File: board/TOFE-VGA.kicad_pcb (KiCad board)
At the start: 2 copper layers, 1 part

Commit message: Started rough layout of pcb
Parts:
- removed U?: TOFE_VGA_Expansion_Board_8x_FullHeight, TOFE_8X_FullHeight
- added C201, C202, C203, C216, C218: 22u, Capacitors_SMD:c_elec_4x5.8, F.Cu at (70.1, 247.0)
- added C204, C205, C206, C207, C208, C209, C210, C211, C212, C213, C219, C220, C221, C301: 100n, Resistors_SMD:R_0805_HandSoldering, F.Cu at (70.1, 247.0)
- added C214: 1u, Capacitors_SMD:c_elec_4x5.8, F.Cu at (70.1, 247.0)
- added C215, C409: 10n, Resistors_SMD:R_0805_HandSoldering, F.Cu at (70.1, 247.0)
- added C217: 2u2, Capacitors_SMD:c_elec_4x5.8, F.Cu at (70.1, 247.0)
- added C401, C402, C403, C404, C405, C406, C407, C408: 47n, Resistors_SMD:R_0805_HandSoldering, F.Cu at (70.1, 247.0)
- added C410: 82n, Resistors_SMD:R_0805_HandSoldering, F.Cu at (100.2, 93.0)
- added C411: 8.2n, Resistors_SMD:R_0805_HandSoldering, F.Cu at (104.2, 93.0)
- added D201, D202, D203, D204, D205, D302, D303, D304: LED, LEDs:LED_0805, F.Cu at (70.1, 247.0)
- added D301: DIODE, Diodes_SMD:SMB_Handsoldering, F.Cu at (70.1, 247.0)
- added JP301: JUMPER, CON-SMD-2.54:HARWIN-M20-87-2x1, F.Cu at (70.1, 247.0)
- added L401, L402, L403, L404, L405, L406: FERRITE, Resistors_SMD:R_0805_HandSoldering, F.Cu at (70.1, 247.0)
- added P301: TOFE I2C, CON-SMD-2.54:HARWIN-M20-87-4x1, F.Cu at (70.1, 247.0)
- added P302: TOFE-8X, TOFE_8X_HalfHeight:TOFE_8X_HalfHeight, F.Cu at (62.2, 154.0)
- added P303: DEBUG, CON-SMD-2.54:TE-AMPMODU-MOD-II-4X2, F.Cu at (102.2, 137.0)
- added P401: AD9984 I2C, CON-SMD-2.54:HARWIN-M20-87-4x1, F.Cu at (130.2, 93.0)
- added P501: VGA RX I2C 3v, CON-SMD-2.54:HARWIN-M20-87-4x1, F.Cu at (70.1, 247.0)
- added P502: VGA TX I2C 3v, CON-SMD-2.54:HARWIN-M20-87-4x1, F.Cu at (70.1, 247.0)
- added P503: VGA RX I2C 5v, CON-SMD-2.54:HARWIN-M20-87-4x1, F.Cu at (70.1, 247.0)
- added P504: VGA TX I2C 5v, CON-SMD-2.54:HARWIN-M20-87-4x1, F.Cu at (70.1, 247.0)
- added P505: DE-15, DE-15:TE-1-1734530-1, F.Cu at (62.2, 120.0)
- added P506: DE-15, DE-15:TE-1-1734530-1, F.Cu at (62.2, 85.0)
- added P601: 3-RCA, 3-RCA:MR-100H, F.Cu at (119.2, 60.0)
- added R201: 470R, Resistors_SMD:R_0805_HandSoldering, F.Cu at (70.1, 247.0)
- added R202, R206: 76K8, Resistors_SMD:R_0805_HandSoldering, F.Cu at (70.1, 247.0)
- added R203, R207: 147K, Resistors_SMD:R_0805_HandSoldering, F.Cu at (70.1, 247.0)
- added R204, R304, R305, R306: 68R, Resistors_SMD:R_0805_HandSoldering, F.Cu at (70.1, 247.0)
- added R205, R209: 1R8, Resistors_SMD:R_0805_HandSoldering, F.Cu at (70.1, 247.0)
- added R208: 150R, Resistors_SMD:R_0805_HandSoldering, F.Cu at (70.1, 247.0)
- added R301, R302, R303: 10K, Resistors_SMD:R_0805_HandSoldering, F.Cu at (70.1, 247.0)
- added R401, R402, R403, R404, R405, R406: 75R, Resistors_SMD:R_0805_HandSoldering, F.Cu at (70.1, 247.0)
- added R407: 1K, Resistors_SMD:R_0805_HandSoldering, F.Cu at (70.1, 247.0)
- added R408: 10K, Resistors_SMD:R_0805_HandSoldering, F.Cu at (112.2, 129.0)
- added R409: 10K, Resistors_SMD:R_0805_HandSoldering, F.Cu at (115.2, 132.0)
- added R410: 1K5, Resistors_SMD:R_0805_HandSoldering, F.Cu at (100.2, 99.0)
- added R411: 1K, Resistors_SMD:R_0805_HandSoldering, F.Cu at (111.2, 94.0)
- added R412: 1K, Resistors_SMD:R_0805_HandSoldering, F.Cu at (115.2, 94.0)
- added R413: 1K, Resistors_SMD:R_0805_HandSoldering, F.Cu at (118.2, 94.0)
- added R414: 1K, Resistors_SMD:R_0805_HandSoldering, F.Cu at (121.2, 94.0)
- added R415: 2k2, Resistors_SMD:R_0805_HandSoldering, F.Cu at (127.2, 86.0)
- added R416: 2K2, Resistors_SMD:R_0805_HandSoldering, F.Cu at (131.2, 85.0)
- added R501, R502, R503, R504: 2K2, Resistors_SMD:R_0805_HandSoldering, F.Cu at (70.1, 247.0)
- added R505, R506, R507, R508: 4K7, Resistors_SMD:R_0805_HandSoldering, F.Cu at (70.1, 247.0)
- added TP401, TP402, TP404: TESTPOINT, SMD_Packages:1Pin, F.Cu at (70.1, 247.0)
- added TP403: TESTPOINT, SMD_Packages:1Pin, F.Cu at (107.2, 184.0)
- added U201, U202: ADP3334, Housings_SSOP:MSOP-8_3x3mm_Pitch0.65mm, F.Cu at (70.1, 247.0)
- added U203: LP2985, TO_SOT_Packages_SMD:SOT-23-5, F.Cu at (70.1, 247.0)
- added U301: 24AA01/24LC01B, TO_SOT_Packages_SMD:SOT-23-5, F.Cu at (70.1, 247.0)
- added U401: AD9984, analog-devices2:analog-devices2-LQFP80, F.Cu at (119.2, 114.0)
- added U501, U502: TCA9617A, Housings_SSOP:MSOP-8_3x3mm_Pitch0.65mm, F.Cu at (70.1, 247.0)
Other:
- board outline added: 46 x 3 mm
- copper layers 2 -> 4
- board text added: "99 x 99mm"

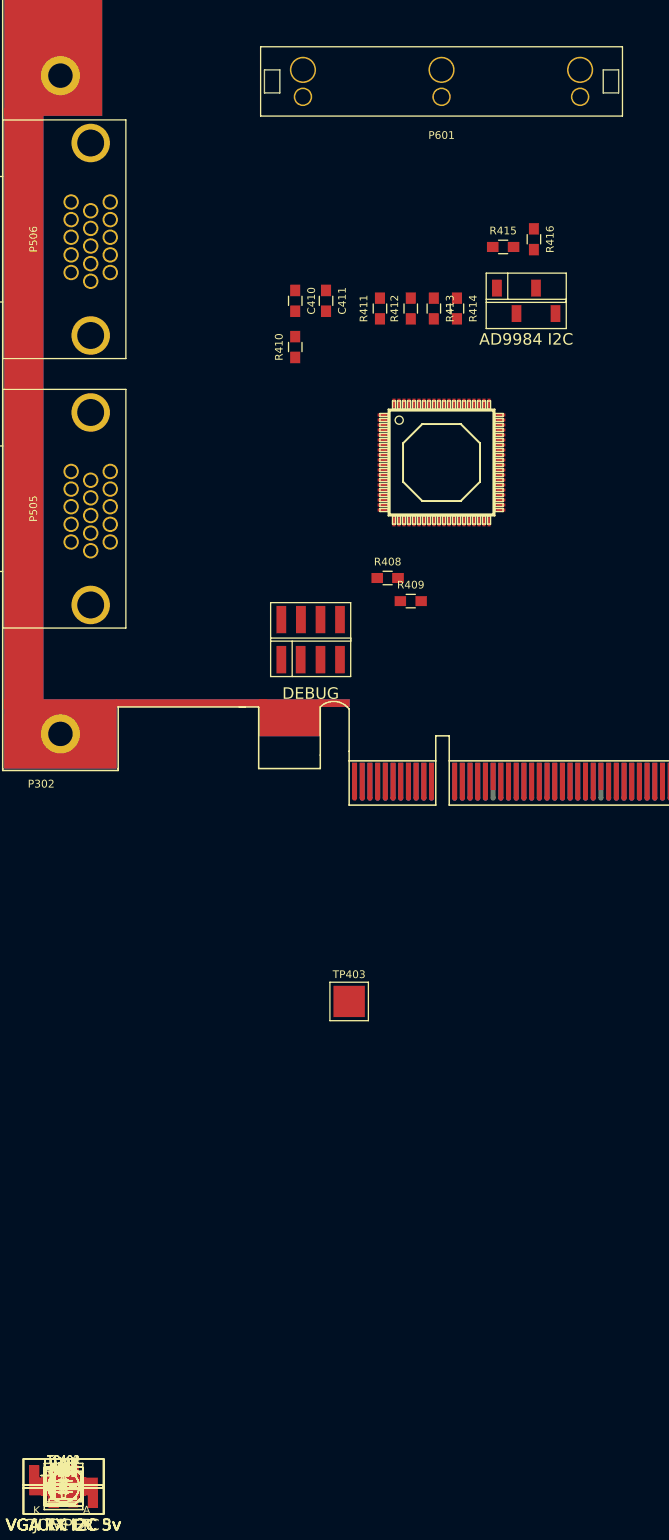
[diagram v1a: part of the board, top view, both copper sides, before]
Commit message: Remove component input to allow design to fit on smaller and much cheaper board
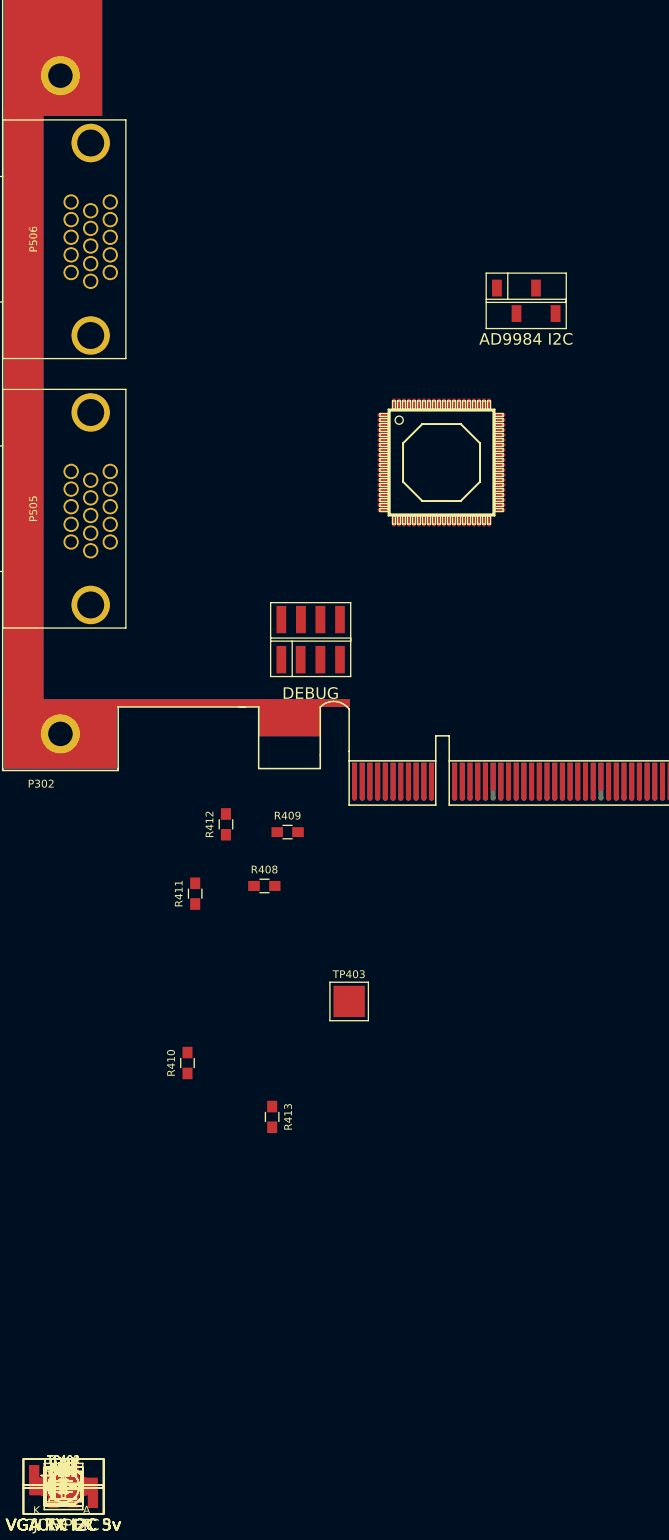
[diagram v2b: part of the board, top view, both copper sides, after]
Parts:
- removed C408: 47n, Resistors_SMD:R_0805_HandSoldering
- removed C409: 10n, Resistors_SMD:R_0805_HandSoldering
- removed C410: 82n, Resistors_SMD:R_0805_HandSoldering
- removed C411: 8.2n, Resistors_SMD:R_0805_HandSoldering
- removed L404, L405, L406: FERRITE, Resistors_SMD:R_0805_HandSoldering
- removed P601: 3-RCA, 3-RCA:MR-100H
- removed R414: 1K, Resistors_SMD:R_0805_HandSoldering
- removed R415: 2k2, Resistors_SMD:R_0805_HandSoldering
- removed R416: 2K2, Resistors_SMD:R_0805_HandSoldering
- C405: value 47n -> 10n
- C406: value 47n -> 82n
- C407: value 47n -> 8.2n
- R404: value 75R -> 1K
- R405, R406: value 75R -> 10K
- R407: value 1K -> 1K5
- R408, R409: value 10K -> 1K
- R410: value 1K5 -> 1K
- R412: value 1K -> 2k2
- R413: value 1K -> 2K2
- moved R413 107.1 mm to (97.2, 199.0)
- moved R410 94.0 mm to (86.2, 192.0)
- moved R411 79.7 mm to (87.2, 170.0)
- moved R412 71.2 mm to (91.2, 161.0)
- moved R408 43.1 mm to (96.2, 169.0)
- moved R409 34.0 mm to (99.2, 162.0)
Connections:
- C403 pad 2: Net-(C403-Pad2) -> Net-(C402-Pad2)
- C404 pad 2: Net-(C403-Pad2) -> Net-(C404-Pad2)
- C406 pad 1: Net-(C406-Pad1) -> PVD
- C406 pad 2: Net-(C405-Pad2) -> Net-(C406-Pad2)
- C407 pad 1: Net-(C407-Pad1) -> PVD
- L402 pad 1: /TOFE-VGA/AD9984/COMP_Pb -> /TOFE-VGA/AD9984/VGA_G
- L403 pad 1: /TOFE-VGA/AD9984/VGA_G -> /TOFE-VGA/AD9984/VGA_R
- L403 pad 2: Net-(C403-Pad2) -> Net-(C404-Pad2)
- R403 pad 1: Net-(C403-Pad2) -> Net-(C404-Pad2)
- R404 pad 1: Net-(C405-Pad2) -> Net-(R404-Pad1)
- R405 pad 1: Net-(C407-Pad2) -> +3V3
- R405 pad 2: GND -> /TOFE-VGA/AD9984/VSOUT
- R406 pad 1: Net-(C408-Pad2) -> /TOFE-VGA/AD9984/VSOUT
- R407 pad 1: Net-(R407-Pad1) -> Net-(C407-Pad2)
- R407 pad 2: GND -> Net-(C406-Pad2)
- R408 pad 1: +3V3 -> Net-(R408-Pad1)
- R408 pad 2: /TOFE-VGA/AD9984/VSOUT -> GND
- R409 pad 1: /TOFE-VGA/AD9984/VSOUT -> Net-(R409-Pad1)
- R410 pad 1: Net-(C411-Pad2) -> GND
- R410 pad 2: Net-(C410-Pad2) -> Net-(R410-Pad2)
- R411 pad 1: Net-(R411-Pad1) -> GND
- R411 pad 2: GND -> Net-(R411-Pad2)
- R412 pad 1: Net-(R412-Pad1) -> +3V3
- R412 pad 2: GND -> /TOFE-VGA/AD9984/SCL_AD9984
- R413 pad 1: GND -> +3V3
- R413 pad 2: Net-(R413-Pad2) -> /TOFE-VGA/AD9984/SDA_AD9984
- TP401 pad 1: Net-(R407-Pad1) -> Net-(R404-Pad1)
- TP403 pad 1: Net-(R411-Pad1) -> Net-(R408-Pad1)
- TP404 pad 1: Net-(R412-Pad1) -> Net-(R409-Pad1)
- U401 pad 10: Net-(C405-Pad1) -> Net-(U401-Pad10)
- U401 pad 12: Net-(C406-Pad1) -> Net-(U401-Pad12)
- U401 pad 14: Net-(C407-Pad1) -> Net-(C404-Pad1)
- U401 pad 17: Net-(R407-Pad1) -> Net-(R404-Pad1)
- U401 pad 18: Net-(C409-Pad2) -> Net-(C405-Pad2)
- U401 pad 20: Net-(C409-Pad1) -> Net-(C405-Pad1)
- U401 pad 4: Net-(C402-Pad1) -> Net-(U401-Pad4)
- U401 pad 6: Net-(C403-Pad1) -> Net-(C402-Pad1)
- U401 pad 68: Net-(R414-Pad2) -> Net-(R411-Pad2)
- U401 pad 69: Net-(R413-Pad2) -> Net-(R410-Pad2)
- U401 pad 72: Net-(R412-Pad1) -> Net-(R409-Pad1)
- U401 pad 73: Net-(R411-Pad1) -> Net-(R408-Pad1)
- U401 pad 78: Net-(C411-Pad2) -> Net-(C407-Pad2)
- U401 pad 8: Net-(C404-Pad1) -> Net-(C403-Pad1)
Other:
- board outline removed

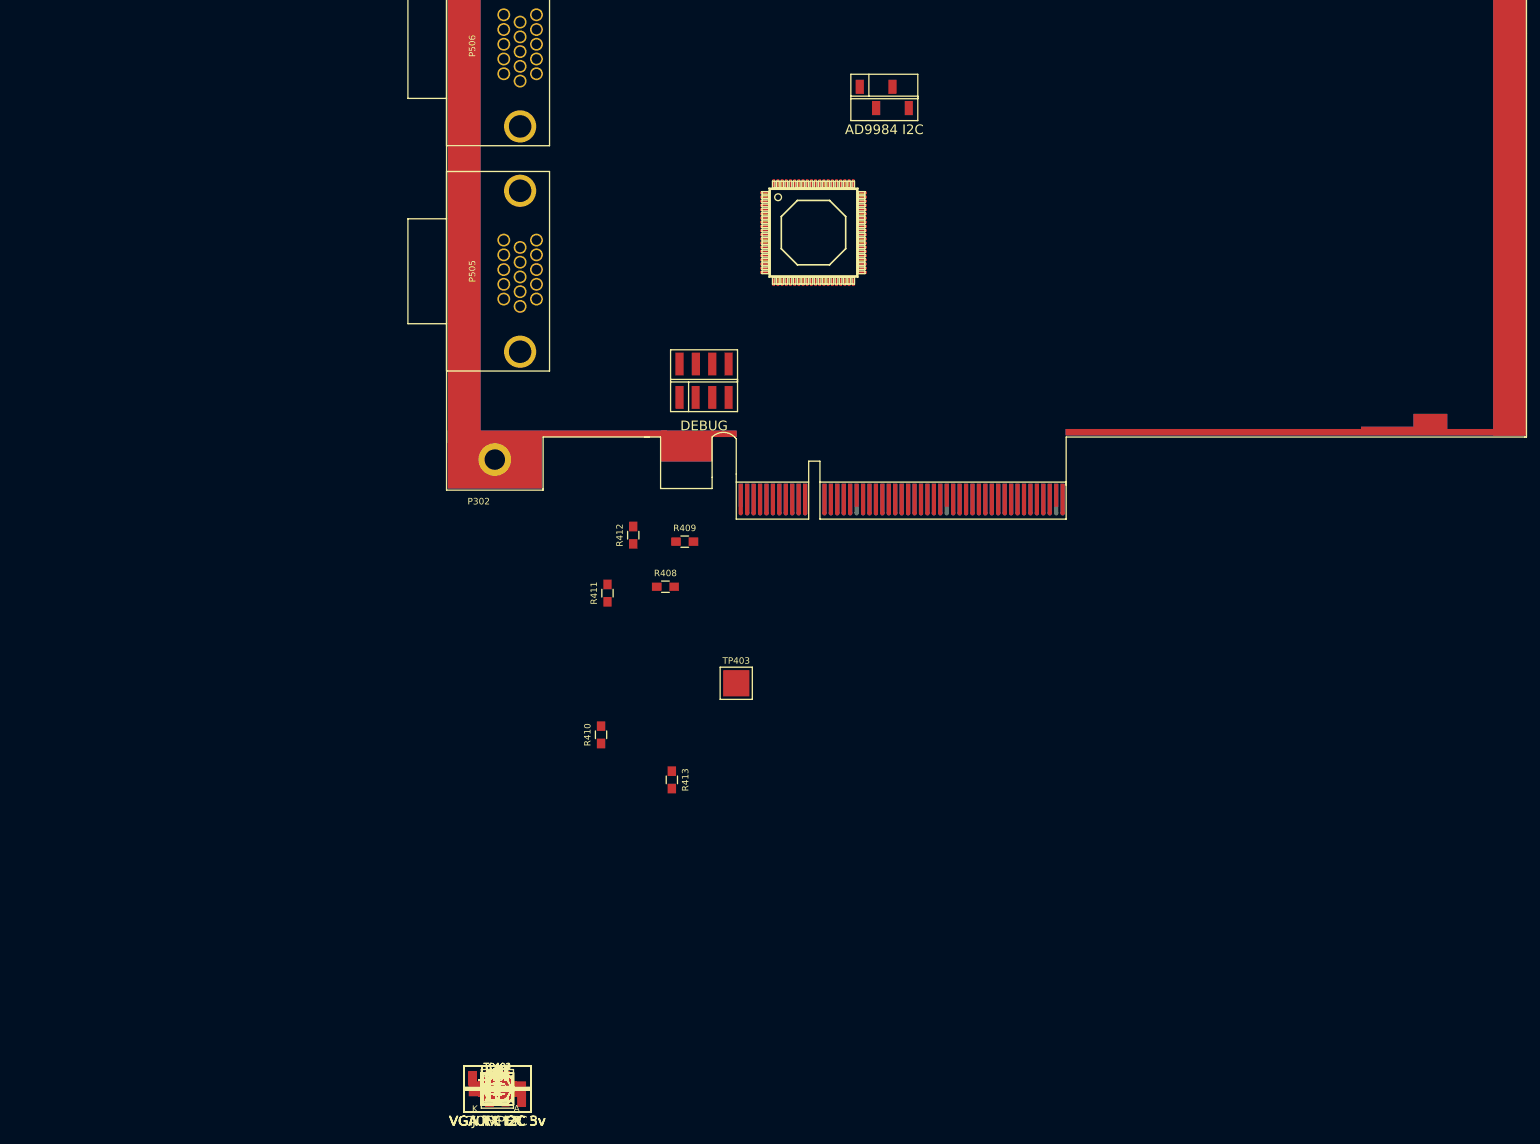
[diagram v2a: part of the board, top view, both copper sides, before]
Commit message: Grouping components together on board
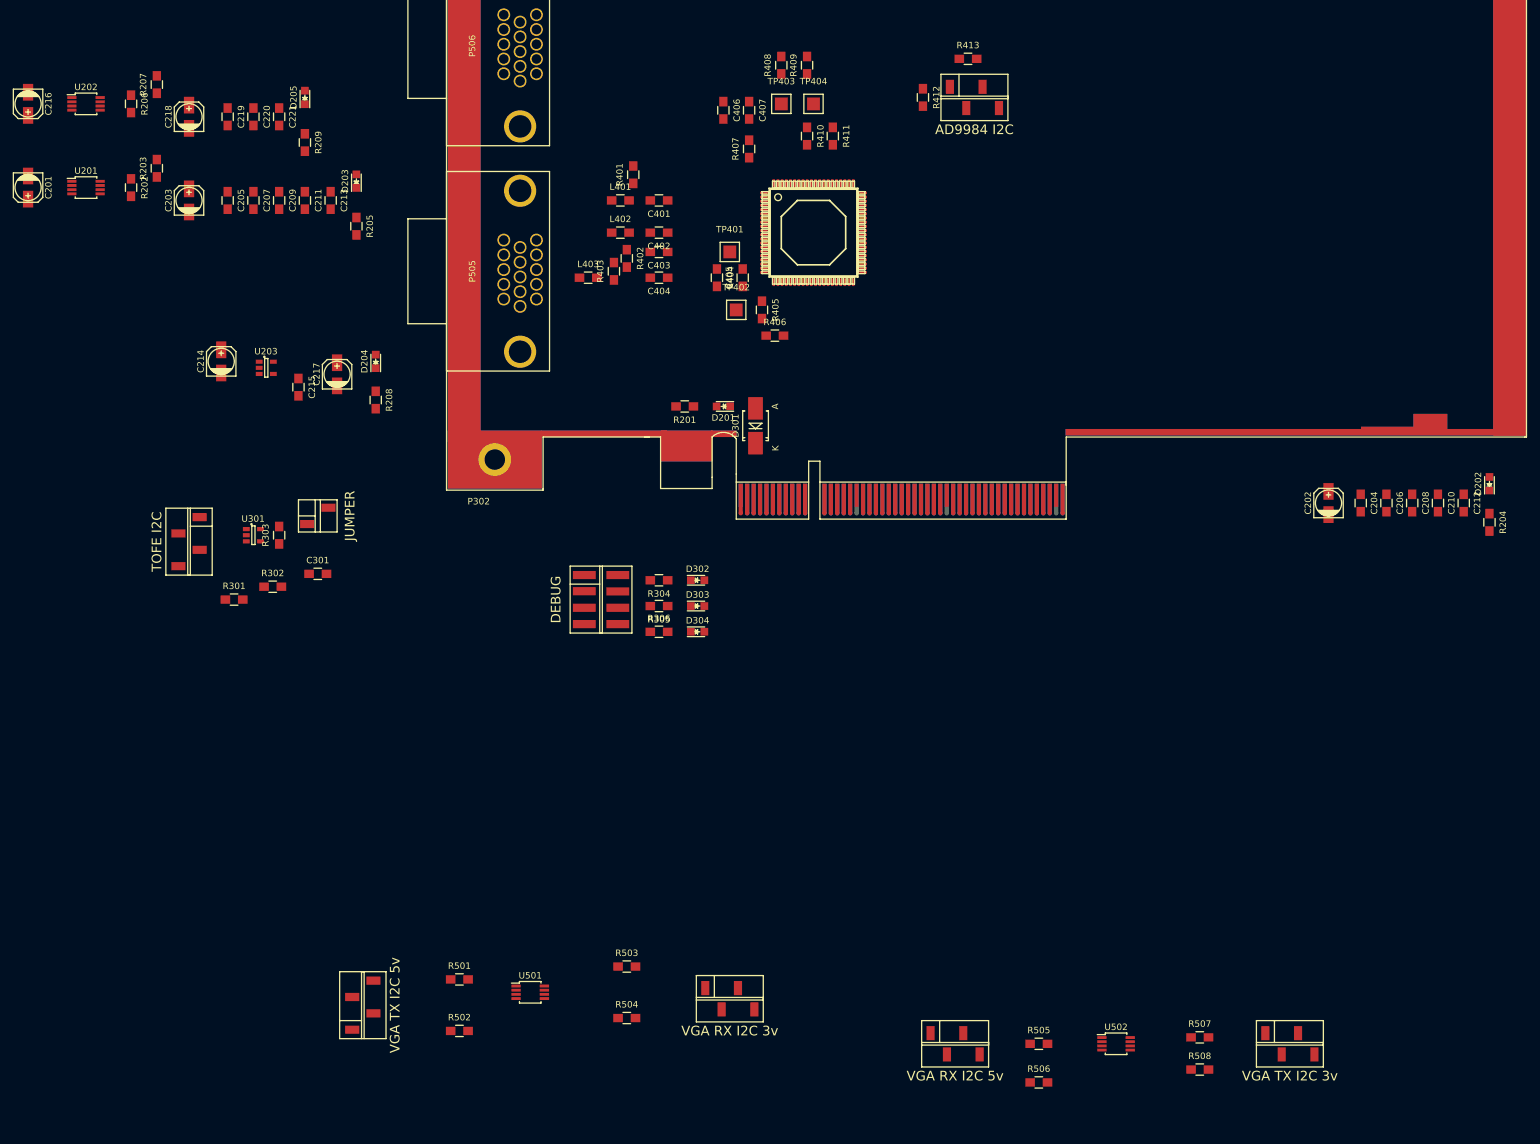
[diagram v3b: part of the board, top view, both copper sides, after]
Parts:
- TP401, TP402, TP403, TP404: footprint SMD_Packages:1Pin -> 2MM-TESTPOINT:2MM-TESTPOINT
- moved D202 180.5 mm to (224.2, 153.0), turned to 90 degrees
- moved R204 177.5 mm to (224.2, 159.0), turned to 270 degrees
- moved C212 175.5 mm to (220.2, 156.0), turned to 270 degrees
- moved C210 172.1 mm to (216.2, 156.0), turned to 270 degrees
- moved C216 169.5 mm to (-2.80, 94.0), turned to 270 degrees
- moved C208 168.7 mm to (212.2, 156.0), turned to 270 degrees
- moved U202 165.8 mm to (6.20, 94.0)
- moved C206 165.4 mm to (208.2, 156.0), turned to 270 degrees
- moved R207 164.7 mm to (17.2, 91.0), turned to 90 degrees
- moved R206 163.2 mm to (13.2, 94.0), turned to 270 degrees
- moved C204 162.1 mm to (204.2, 156.0), turned to 270 degrees
- moved TP404 160.7 mm to (119.2, 94.0)
- moved C218 158.4 mm to (22.2, 96.0), turned to 90 degrees
- moved C202 157.9 mm to (199.2, 156.0), turned to 90 degrees
- moved C201 157.8 mm to (-2.80, 107.0), turned to 270 degrees
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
